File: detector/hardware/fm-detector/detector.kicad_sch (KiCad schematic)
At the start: 33 parts, among them Q4 MMBT3904, Q5 MMBT3904, Q6 MMBT3904, Q7 MMBT3904, Q8 MMBT3904

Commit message: pulse detector design
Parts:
- removed C19: 10µ, g-cap:C_1210_3225Metric, symbol #gplm:cap/CAP-0003-1005
- removed C20: 470n, g-cap:C_0603_1608Metric, symbol #gplm:cap/CAP-0000-0474
- removed C21, C22, C23: 390p, g-cap:C_0603_1608Metric, symbol #gplm:cap/CAP-0000-0391
- removed C24: 10n, g-cap:C_0603_1608Metric, symbol #gplm:cap/CAP-0000-0103
- removed Q8: MMBT3904, g-SOT:SOT-23-3, symbol #gplm:trs/TRS-0000-0001
- removed R22: 0E, g-res:R_0603_1608Metric, symbol #gplm:res/RES-0000-0000
- removed R23, R24: 470K, g-res:R_0603_1608Metric, symbol #gplm:res/RES-0000-4703
- removed R25, R26, R27: 15K, g-res:R_0603_1608Metric, symbol #gplm:res/RES-0000-1502
- removed R28: 8K2, g-res:R_0603_1608Metric, symbol #gplm:res/RES-0000-8201
- removed R29: 2K2, g-res:R_0603_1608Metric, symbol #gplm:res/RES-0000-2201
- added D8: 1N4148, g-dio:D_SOD-323, symbol #gplm:dio/DIO-0001-0000
- C15, C16, C17: Voltage 50V -> 50
- C18: value 330p -> 150p; symbol #gplm:cap/CAP-0000-0331 -> #gplm:cap/CAP-0000-0151; Capacitance 330p -> 150p; IPN CAP-0000-0331 -> CAP-0000-0151; LCSC C1664 -> C519499; MPN CL10C331JB8NNNC -> CC0603FRNPO9BN151; Manufacturer Samsung Electro-Mechanics -> YAGEO; Tolerance ±5% -> ±1%; Voltage 50V -> 50
- R21: value 20K -> 10K; symbol #gplm:res/RES-0000-2002 -> #gplm:res/RES-0000-1002; IPN RES-0000-2002 -> RES-0000-1002; LCSC C4184 -> C25804; MPN RC0603FR-0720KL -> RC0603FR-0710KL; Resistance 20K -> 10K
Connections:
- net PWM_AUDIO: now also D8.1 (K)
- net at Q6.1 (B), R21.1: now also D8.2 (A)
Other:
- note removed: "(1.30 Vdc)"
- note removed: "(1.94 Vdc)"
- note removed: "(2.05 Vdc)"
- moved on the sheet: C15, C16, C17, C18, D2, Q4, Q5, Q6, Q7, R13, R14, R15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

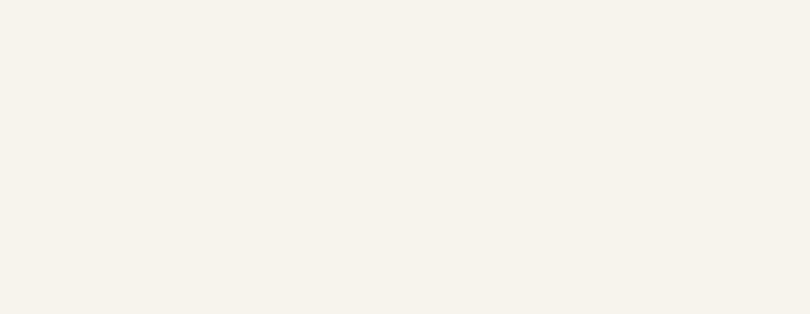
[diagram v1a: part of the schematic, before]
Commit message: Schematic for PCB-0010-0100
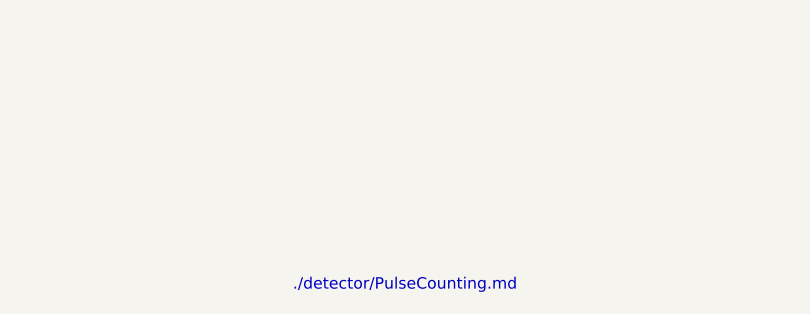
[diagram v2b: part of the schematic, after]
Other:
- note added: "./detector/PulseCounting.md"
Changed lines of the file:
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@@
+		)
+	)
+	(text "./detector/PulseCounting.md"
+		(exclude_from_sim no)
+		(at 115.57 129.54 0)
+		(effects
+			(font
+				(size 1.27 1.27)
+			)
+			(href "https://github.com/LieBtrau/MegawattKS_Radio_Design_101/blob/main/detector/PulseCounting.md")
 		)
 	)
